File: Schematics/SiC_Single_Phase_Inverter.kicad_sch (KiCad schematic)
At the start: 2 parts, among them J1 23AH8785-Black, J2 23AH8786-Red

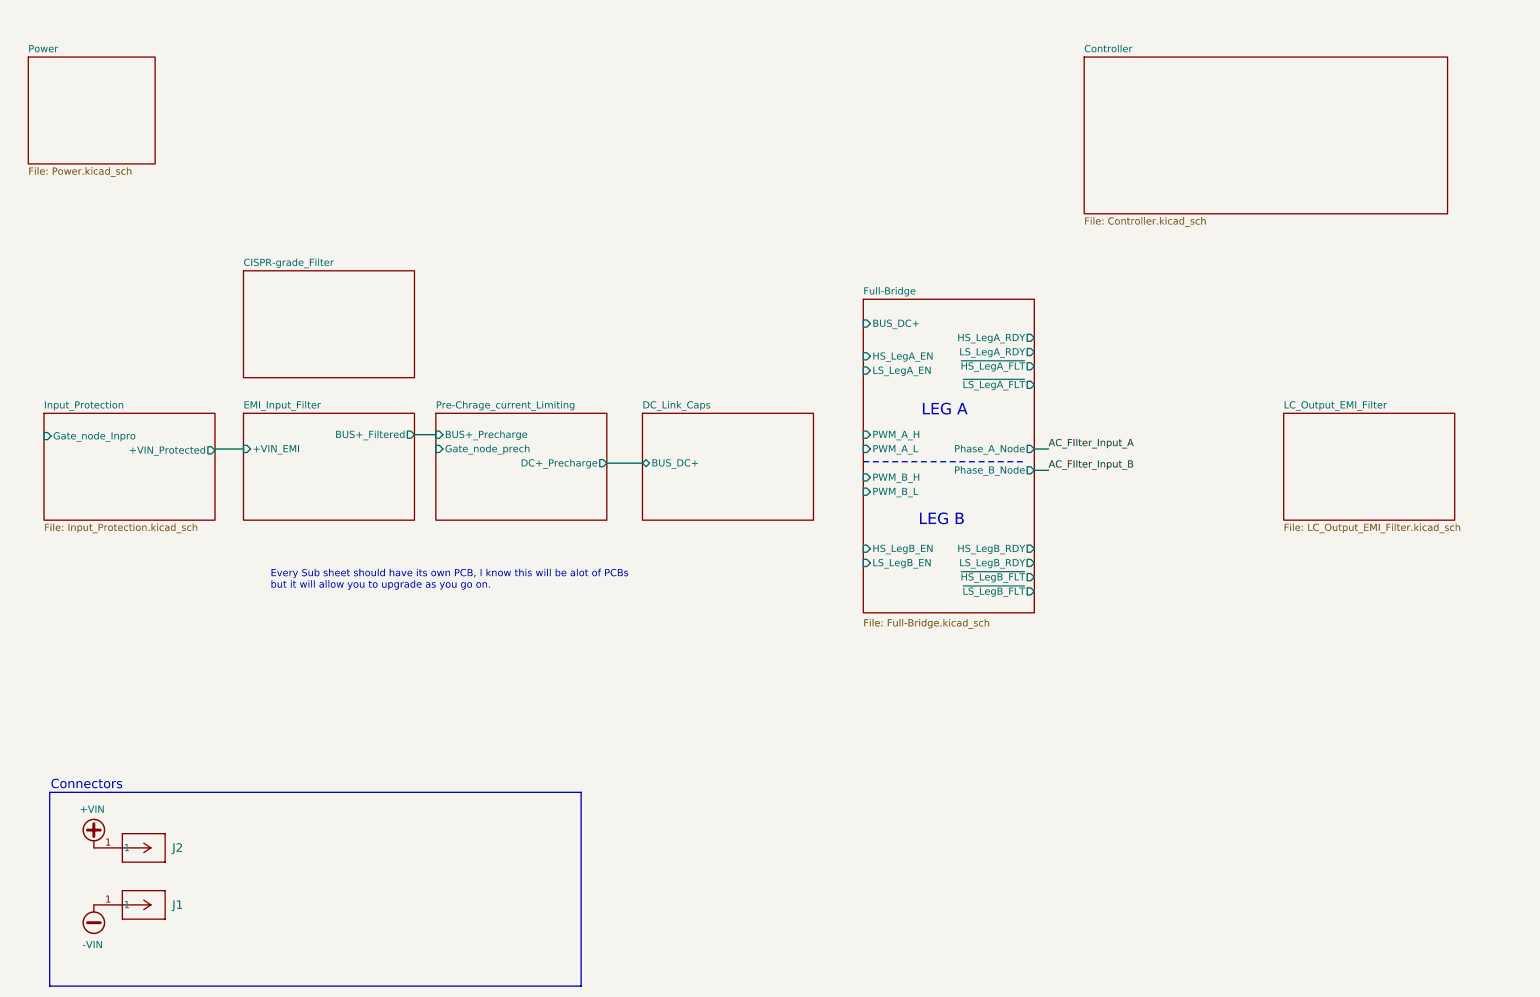
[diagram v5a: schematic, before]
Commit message: Added LCL filter to output EMI Filter
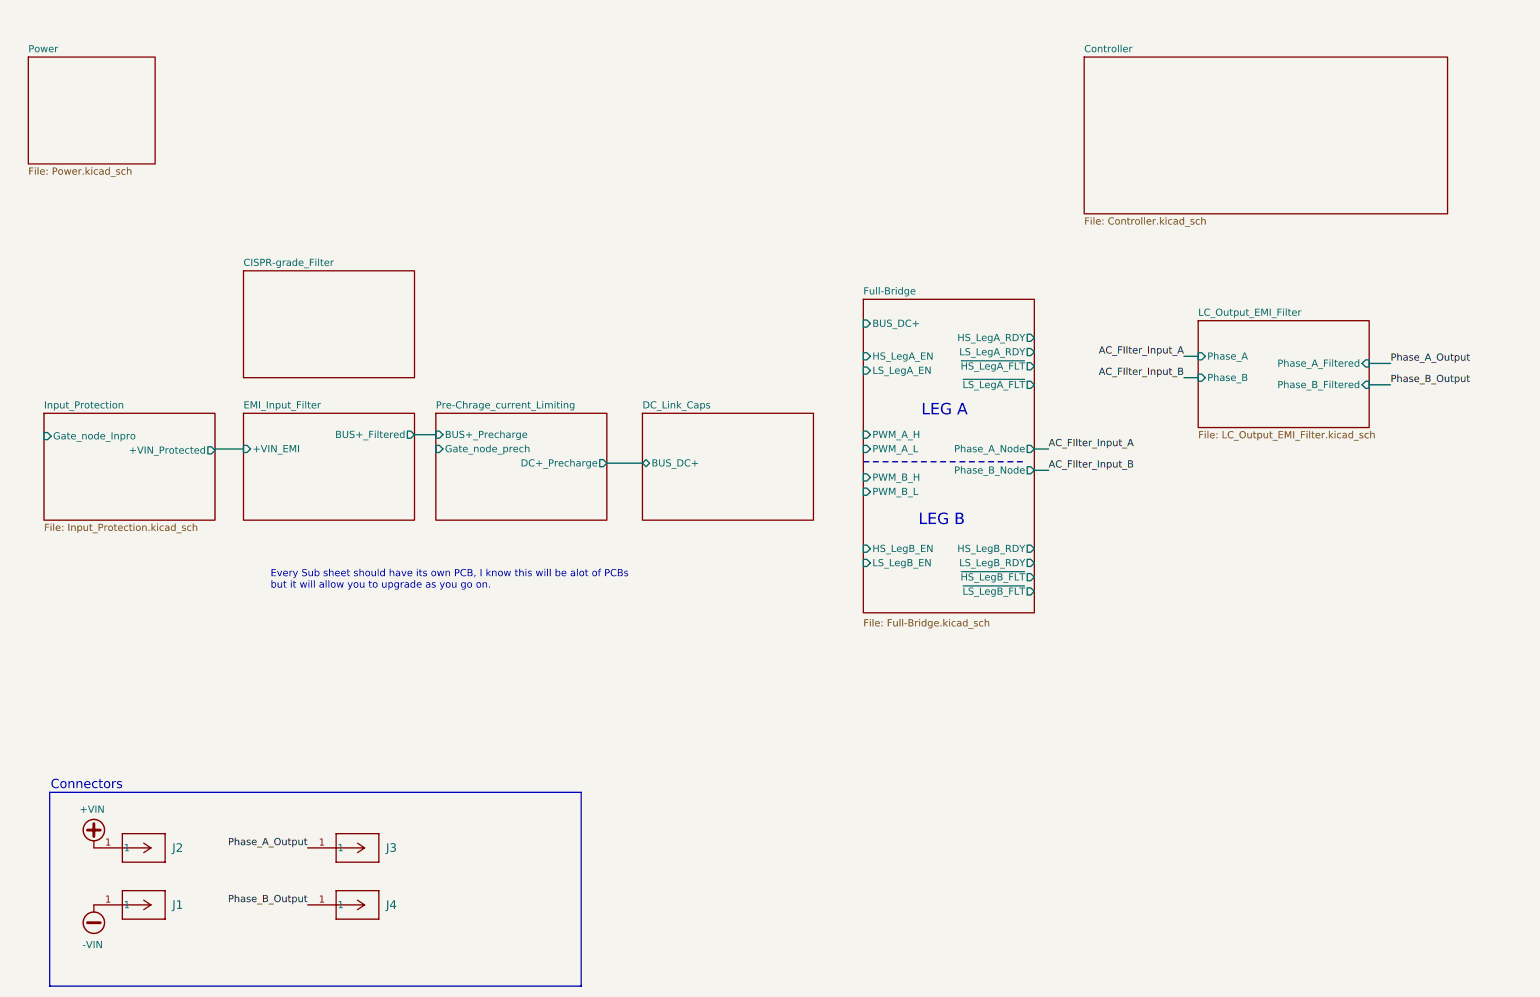
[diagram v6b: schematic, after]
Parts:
- added J3: 23AH8786-Red, SiC_Inverter:23AH8786-Red, symbol SiC_Inverter:23AH8786-Red
- added J4: 23AH8785-Black, SiC_Inverter:23AH8785-Black, symbol SiC_Inverter:23AH8785-Black
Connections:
- new net Phase_A_Output: J3.1
- new net Phase_B_Output: J4.1
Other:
- sheet LC_Output_EMI_Filter ports: added Phase_A, Phase_A_Filtered, Phase_B, Phase_B_Filtered; removed none

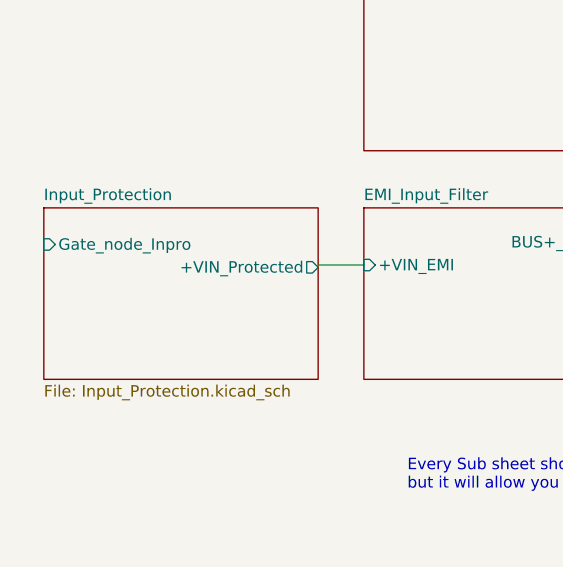
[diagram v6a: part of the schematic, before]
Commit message: [WIP SiC Single Phase Inverter
- Updated README.md
- Added New Parts for Output filter L,C,R
- Added datasheets for the new parts
- Added 3D models for the new parts
- Added new symbols and footprints for the L,C,R
- Finished output filter
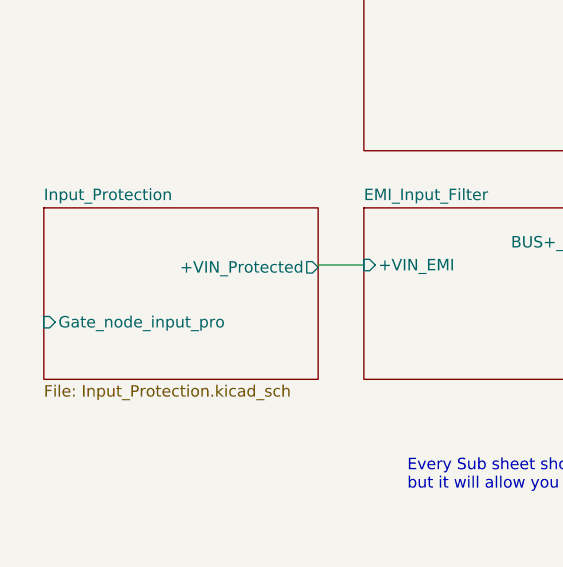
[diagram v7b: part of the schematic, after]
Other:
- sheet Input_Protection ports: added Gate_node_input_pro; removed Gate_node_Inpro
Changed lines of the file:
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@@
 			)
 		)
-		(pin "Gate_node_Inpro" input
-			(at 25.4 89.154 180)
+		(pin "Gate_node_input_pro" input
+			(at 25.4 97.79 180)
 			(effects
 				(font

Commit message: Changing Text to Text Block
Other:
- note removed: "Connectors"
- note removed: "Every Sub sheet should have its own PCB, I know this will be alot of PCBs but it will allow you to upgrade as you go on."
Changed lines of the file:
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@@
-		)
-	)
-	(text "Every Sub sheet should have its own PCB, I know this will be alot of PCBs\nbut it will allow you to upgrade as you go on.\n"
-		(exclude_from_sim no)
-		(at 65.786 114.808 0)
-		(effects
-			(font
-				(size 1.27 1.27)
-			)
-			(justify left)
-		)
-	)
-	(text "Connectors"
-		(exclude_from_sim no)
-		(at 33.02 151.384 0)
-		(effects
-			(font
-				(size 1.651 1.651)
-			)
 		)
 	)
@@
 		)
 	)
+	(text_box "Add Testing Points"
+		(exclude_from_sim no)
+		(at 65.278 114.554 0)
+		(size 21.336 4.826)
+		(margins 0.9525 0.9525 0.9525 0.9525)
+		(stroke
+			(width 0)
+			(type solid)
+		)
+		(fill
+			(type color)
+			(color 0 0 255 0.1)
+		)
+		(effects
+			(font
+				(size 1.27 1.27)
+			)
+			(justify left top)
+		)
+	)
+	(text_box "Connectors"
+		(exclude_from_sim no)
+		(at 26.416 149.352 0)
+		(size 12.446 3.048)
+		(margins 0.9525 0.9525 0.9525 0.9525)
+		(stroke
+			(width 0)
+			(type solid)
+		)
+		(fill
+			(type color)
+			(color 0 0 255 0.1)
+		)
+		(effects
+			(font
+				(size 1.27 1.27)
+			)
+			(justify left top)
+		)
+	)
